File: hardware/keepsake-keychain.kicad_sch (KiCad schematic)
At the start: 95 parts, among them Q1 MMFTP4042K, Q2 MMFTP4042K, Q3 MMFTP4042K, Q4 MMFTP4042K, SW1 SPDT Power Switch, SW2 PTS636 SK25J SMTR LFS, U1 74HC595, U2 74HC595, U3 74HC595, U4 Op Amp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

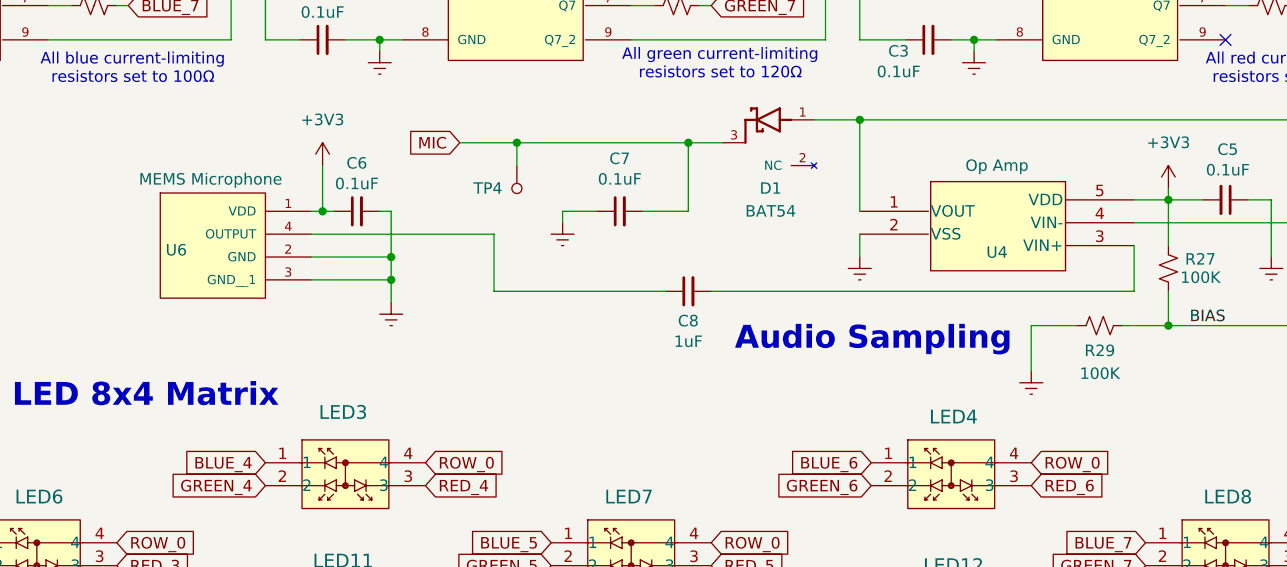
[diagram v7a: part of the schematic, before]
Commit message: Route first half of LED traces
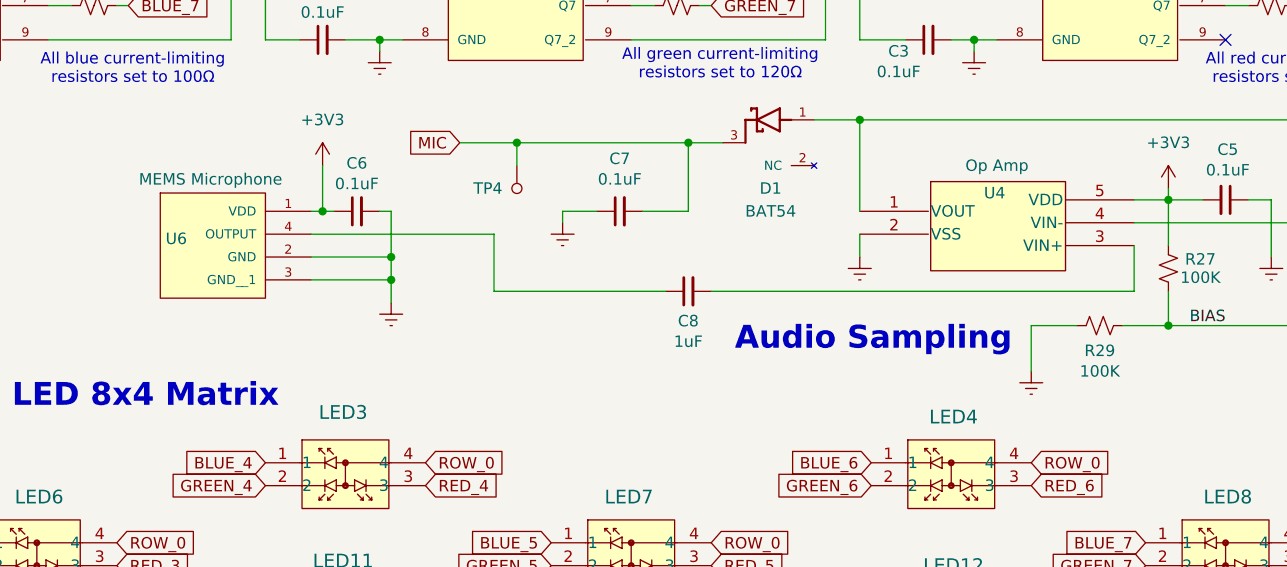
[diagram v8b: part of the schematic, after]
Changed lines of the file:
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@@
 		(dnp no)
 		(property "Reference" "U4"
-			(at 238.76 76.962 0)
+			(at 238.506 70.358 0)
 			(effects
 				(font
@@
 		)
 		(property "Value" "100K"
-			(at 250.19 90.424 90)
+			(at 250.19 90.17 90)
 			(effects
 				(font
@@
 		(dnp no)
 		(property "Reference" "U6"
-			(at 147.574 76.708 0)
+			(at 147.574 75.438 0)
 			(effects
 				(font
